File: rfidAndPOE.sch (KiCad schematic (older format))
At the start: 51 parts, among them Q1 Si3440DV, NFET, Q2 MMBTA42, Q3 2N7002

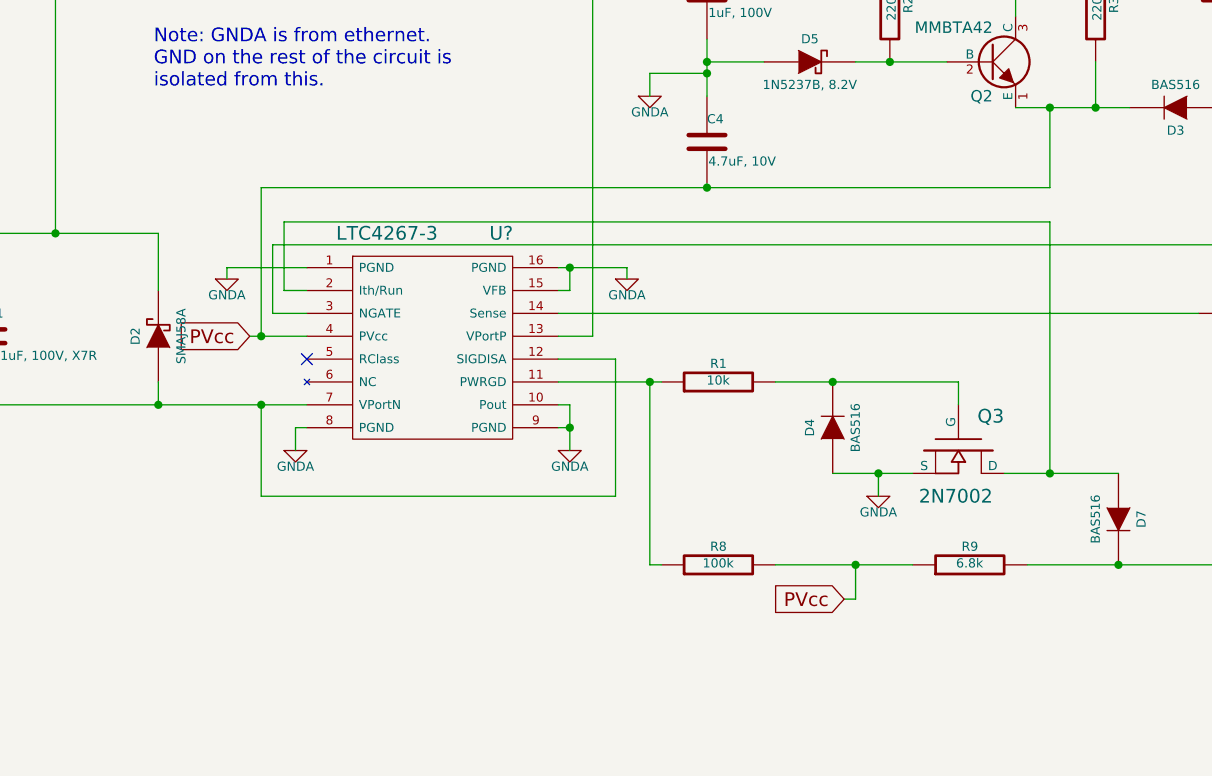
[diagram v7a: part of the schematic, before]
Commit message: Changed PVcc from a global flag to just a label and removed some of it's lines to make the schematic clearer.
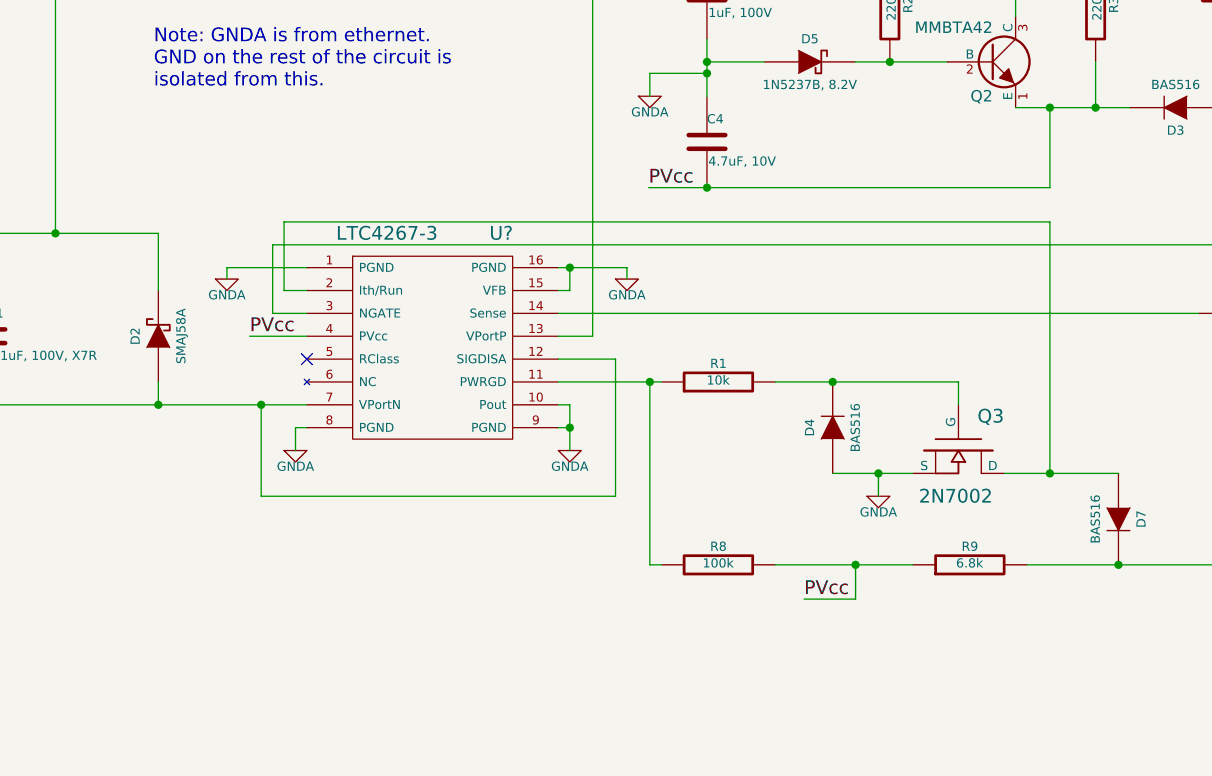
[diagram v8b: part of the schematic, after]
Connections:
- wire segments 115 -> 114
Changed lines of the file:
@@
 	0    -1   -1   0
 $EndComp
-Text GLabel 6085 2740 0    60   Input ~ 0
-PVcc
-Text GLabel 8685 3890 0    60   Input ~ 0
-PVcc
 $Comp
 L OPTOISOLATOR U?
@@
 Connection ~ 8085 1590
 Wire Wire Line
-	6135 2090 9585 2090
-Wire Wire Line
-	6135 2090 6135 2740
-Wire Wire Line
 	6085 2740 6335 2740
 Wire Wire Line
@@
 Connection ~ 9585 3340
 Wire Wire Line
-	8685 3890 8735 3890
+	8510 3890 8735 3890
 Wire Wire Line
 	8735 3890 8735 3740
 Connection ~ 8735 3740
-Connection ~ 6135 2740
 Connection ~ 9885 3740
 Wire Wire Line
@@
 Wire Wire Line
 	13790 1490 13790 1420
+Text Label 6085 2740 0    60   ~ 0
+PVcc
+Text Label 7830 2090 0    60   ~ 0
+PVcc
+Wire Wire Line
+	7830 2090 9585 2090
+Text Label 8510 3890 0    60   ~ 0
+PVcc
 $EndSCHEMATC
